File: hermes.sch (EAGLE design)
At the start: 36 parts

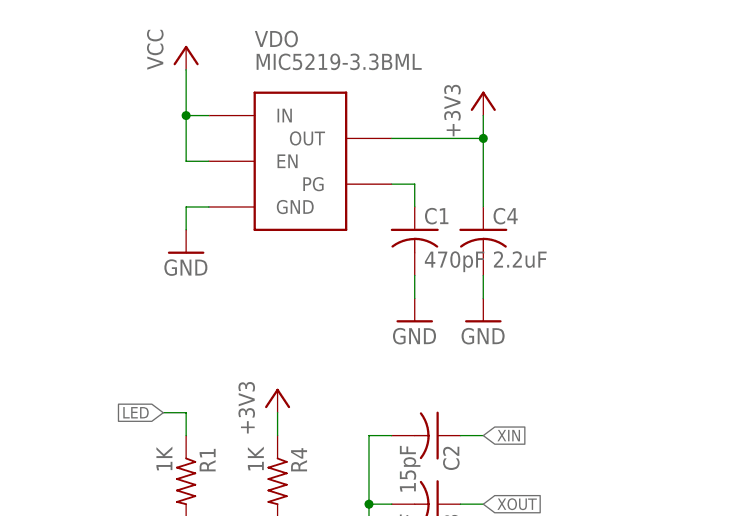
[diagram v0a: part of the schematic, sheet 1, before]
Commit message: Alternative version with LDO TS9013
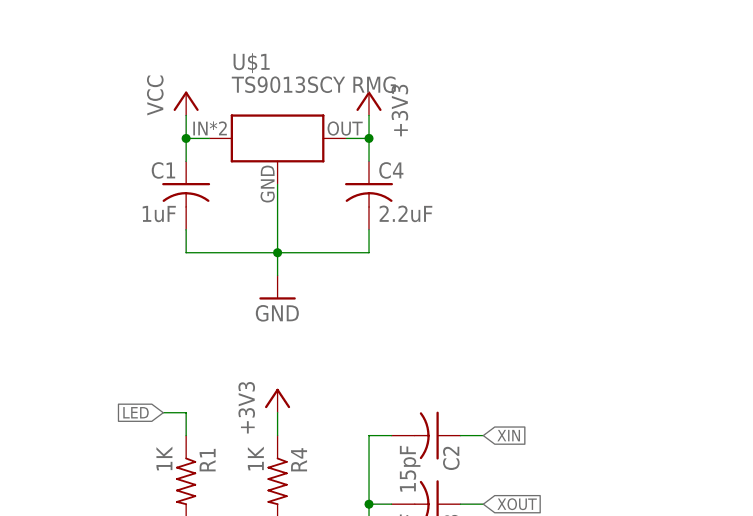
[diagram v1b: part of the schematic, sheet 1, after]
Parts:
- added U$1: TS9013SCY RMG, Hermes_lib:TS9013S
- C1: value 470pF -> 1uF
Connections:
- removed net N$2: C1.1, VDOG$1.PG
- net +3V3: now also U$1.P$2; no longer VDOG$1.OUT
- net GND: now also U$1.P$3; no longer VDOG$1.GND
- net VCC: now also C1.1, U$1.P$1; no longer VDOG$1.EN, VDOG$1.IN
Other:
- moved on the sheet: C1, C4
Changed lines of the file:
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@@
 <part name="P+1" library="supply1" library_urn="urn:adsk.eagle:library:371" deviceset="VCC" device=""/>
 <part name="GND8" library="supply1" library_urn="urn:adsk.eagle:library:371" deviceset="GND" device=""/>
-<part name="GND1" library="supply1" library_urn="urn:adsk.eagle:library:371" deviceset="GND" device=""/>
 <part name="+3V34" library="supply1" library_urn="urn:adsk.eagle:library:371" deviceset="+3V3" device=""/>
 <part name="LED1" library="eagle-ltspice" library_urn="urn:adsk.eagle:library:217" deviceset="LED_E" device="SML0603" package3d_urn="urn:adsk.eagle:package:13315/1"/>
@@
 <part name="FRAME2" library="frames" library_urn="urn:adsk.eagle:library:229" deviceset="A4L-LOC" device=""/>
 <part name="FRAME1" library="frames" library_urn="urn:adsk.eagle:library:229" deviceset="A4L-LOC" device=""/>
-<part name="C1" library="rcl" library_urn="urn:adsk.eagle:library:334" deviceset="C-US" device="C0201" package3d_urn="urn:adsk.eagle:package:23690/1" value="470pF"/>
-<part name="GND7" library="supply1" library_urn="urn:adsk.eagle:library:371" deviceset="GND" device=""/>
+<part name="C1" library="rcl" library_urn="urn:adsk.eagle:library:334" deviceset="C-US" device="C0201" package3d_urn="urn:adsk.eagle:package:23690/1" value="1uF"/>
 <part name="XTAL" library="Hermes_lib" deviceset="LFXTAL059596CUTT" device=""/>
 <part name="GND6" library="supply1" library_urn="urn:adsk.eagle:library:371" deviceset="GND" device=""/>
@@
 <part name="SLAVE" library="Hermes_lib" deviceset="PICO-BLADE8" device=""/>
 <part name="GND14" library="supply1" library_urn="urn:adsk.eagle:library:371" deviceset="GND" device=""/>
+<part name="U$1" library="Hermes_lib" deviceset="TS9013" device="S" value="TS9013SCY RMG "/>
 </parts>
 <sheets>
@@
 <instance part="C11" gate="G$1" x="172.72" y="139.7" rot="R90"/>
 <instance part="C9" gate="G$1" x="121.92" y="139.7" rot="R270"/>
-<instance part="VDO" gate="G$1" x="38.1" y="147.32"/>
-<instance part="C4" gate="G$1" x="58.42" y="139.7"/>
-<instance part="P+1" gate="VCC" x="25.4" y="160.02"/>
-<instance part="GND8" gate="1" x="58.42" y="129.54"/>
-<instance part="GND1" gate="1" x="25.4" y="137.16"/>
-<instance part="+3V34" gate="G$1" x="58.42" y="154.94"/>
+<instance part="C4" gate="G$1" x="45.72" y="144.78"/>
+<instance part="P+1" gate="VCC" x="25.4" y="154.94"/>
+<instance part="GND8" gate="1" x="35.56" y="132.08"/>
+<instance part="+3V34" gate="G$1" x="45.72" y="154.94" rot="MR0"/>
 <instance part="LED1" gate="G$1" x="25.4" y="101.6"/>
 <instance part="LED2" gate="G$1" x="35.56" y="101.6"/>
@@
 <instance part="R6" gate="G$1" x="48.26" y="68.58" rot="R90"/>
 <instance part="FRAME1" gate="G$1" x="0" y="0"/>
-<instance part="C1" gate="G$1" x="50.8" y="139.7"/>
-<instance part="GND7" gate="1" x="50.8" y="129.54"/>
+<instance part="C1" gate="G$1" x="25.4" y="144.78" rot="MR0"/>
 <instance part="XTAL" gate="G$1" x="53.34" y="97.79" rot="R180"/>
 <instance part="GND6" gate="1" x="45.72" y="91.44"/>
@@
 <instance part="GND14" gate="1" x="187.96" y="45.72"/>
 <instance part="VDO" gate="-DICE" x="185.42" y="66.04" rot="R180"/>
+<instance part="U$1" gate="G$1" x="35.56" y="149.86"/>
 </instances>
 <busses>
@@
 </segment>
 <segment>
-<pinref part="VDO" gate="G$1" pin="OUT"/>
 <pinref part="C4" gate="G$1" pin="1"/>
-<wire x1="48.26" y1="149.86" x2="58.42" y2="149.86" width="0.1524" layer="91"/>
-<wire x1="58.42" y1="149.86" x2="58.42" y2="142.24" width="0.1524" layer="91"/>
+<wire x1="45.72" y1="152.4" x2="45.72" y2="149.86" width="0.1524" layer="91"/>
 <pinref part="+3V34" gate="G$1" pin="+3V3"/>
-<wire x1="58.42" y1="152.4" x2="58.42" y2="149.86" width="0.1524" layer="91"/>
-<junction x="58.42" y="149.86"/>
+<pinref part="U$1" gate="G$1" pin="P$2"/>
+<wire x1="45.72" y1="149.86" x2="45.72" y2="147.32" width="0.1524" layer="91"/>
+<wire x1="43.18" y1="149.86" x2="45.72" y2="149.86" width="0.1524" layer="91"/>
+<junction x="45.72" y="149.86"/>
 </segment>
 <segment>
@@
 <pinref part="C4" gate="G$1" pin="2"/>
 <pinref part="GND8" gate="1" pin="GND"/>
-<wire x1="58.42" y1="134.62" x2="58.42" y2="132.08" width="0.1524" layer="91"/>
-</segment>
-<segment>
-<pinref part="GND1" gate="1" pin="GND"/>
-<pinref part="VDO" gate="G$1" pin="GND"/>
-<wire x1="25.4" y1="142.24" x2="25.4" y2="139.7" width="0.1524" layer="91"/>
-<wire x1="27.94" y1="142.24" x2="25.4" y2="142.24" width="0.1524" layer="91"/>
+<wire x1="45.72" y1="139.7" x2="45.72" y2="137.16" width="0.1524" layer="91"/>
+<wire x1="45.72" y1="137.16" x2="35.56" y2="137.16" width="0.1524" layer="91"/>
+<wire x1="35.56" y1="137.16" x2="35.56" y2="134.62" width="0.1524" layer="91"/>
+<pinref part="C1" gate="G$1" pin="2"/>
+<wire x1="25.4" y1="139.7" x2="25.4" y2="137.16" width="0.1524" layer="91"/>
+<wire x1="25.4" y1="137.16" x2="35.56" y2="137.16" width="0.1524" layer="91"/>
+<junction x="35.56" y="137.16"/>
+<pinref part="U$1" gate="G$1" pin="P$3"/>
+<wire x1="35.56" y1="144.78" x2="35.56" y2="137.16" width="0.1524" layer="91"/>
 </segment>
 <segment>
@@
 <wire x1="45.72" y1="106.68" x2="45.72" y2="109.22" width="0.1524" layer="91"/>
 <junction x="45.72" y="109.22"/>
-</segment>
-<segment>
-<pinref part="C1" gate="G$1" pin="2"/>
-<pinref part="GND7" gate="1" pin="GND"/>
-<wire x1="50.8" y1="134.62" x2="50.8" y2="132.08" width="0.1524" layer="91"/>
 </segment>
 <segment>
@@
 <segment>
 <pinref part="P+1" gate="VCC" pin="VCC"/>
-<pinref part="VDO" gate="G$1" pin="IN"/>
-<wire x1="27.94" y1="152.4" x2="25.4" y2="152.4" width="0.1524" layer="91"/>
-<wire x1="25.4" y1="152.4" x2="25.4" y2="157.48" width="0.1524" layer="91"/>
-<wire x1="25.4" y1="152.4" x2="25.4" y2="147.32" width="0.1524" layer="91"/>
-<wire x1="25.4" y1="147.32" x2="27.94" y2="147.32" width="0.1524" layer="91"/>
-<junction x="25.4" y="152.4"/>
-<pinref part="VDO" gate="G$1" pin="EN"/>
+<wire x1="25.4" y1="149.86" x2="25.4" y2="152.4" width="0.1524" layer="91"/>
+<pinref part="U$1" gate="G$1" pin="P$1"/>
+<wire x1="27.94" y1="149.86" x2="25.4" y2="149.86" width="0.1524" layer="91"/>
+<pinref part="C1" gate="G$1" pin="1"/>
+<wire x1="25.4" y1="147.32" x2="25.4" y2="149.86" width="0.1524" layer="91"/>
+<junction x="25.4" y="149.86"/>
 </segment>
 <segment>
@@
 </segment>
 </net>
-<net name="N$2" class="0">
-<segment>
-<pinref part="VDO" gate="G$1" pin="PG"/>
-<pinref part="C1" gate="G$1" pin="1"/>
-<wire x1="48.26" y1="144.78" x2="50.8" y2="144.78" width="0.1524" layer="91"/>
-<wire x1="50.8" y1="144.78" x2="50.8" y2="142.24" width="0.1524" layer="91"/>
-</segment>
-</net>

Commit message: Updated CAM and BOM according to new parts used
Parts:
- removed VDO: MIC5219-3.3BML, Hermes_lib:MIC5219-3.3BML
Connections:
- net GND: no longer VDO-DICE.P$1
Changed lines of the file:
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@@
 <part name="C11" library="rcl" library_urn="urn:adsk.eagle:library:334" deviceset="C-US" device="C0201" package3d_urn="urn:adsk.eagle:package:23690/1" value="1uF"/>
 <part name="C9" library="rcl" library_urn="urn:adsk.eagle:library:334" deviceset="C-US" device="C0201" package3d_urn="urn:adsk.eagle:package:23690/1" value="100nF"/>
-<part name="VDO" library="Hermes_lib" deviceset="MIC5219-" device="3.3BML"/>
 <part name="C4" library="rcl" library_urn="urn:adsk.eagle:library:334" deviceset="C-US" device="C0201" package3d_urn="urn:adsk.eagle:package:23690/1" value="2.2uF"/>
 <part name="P+1" library="supply1" library_urn="urn:adsk.eagle:library:371" deviceset="VCC" device=""/>
@@
 <instance part="SLAVE" gate="-DICE" x="185.42" y="50.8" rot="R180"/>
 <instance part="GND14" gate="1" x="187.96" y="45.72"/>
-<instance part="VDO" gate="-DICE" x="185.42" y="66.04" rot="R180"/>
 <instance part="U$1" gate="G$1" x="35.56" y="149.86"/>
 </instances>
@@
 <wire x1="185.42" y1="50.8" x2="187.96" y2="50.8" width="0.1524" layer="91"/>
 <junction x="187.96" y="50.8"/>
-<pinref part="VDO" gate="-DICE" pin="P$1"/>
-<wire x1="185.42" y1="66.04" x2="187.96" y2="66.04" width="0.1524" layer="91"/>
-<wire x1="187.96" y1="66.04" x2="187.96" y2="60.96" width="0.1524" layer="91"/>
-<junction x="187.96" y="60.96"/>
 </segment>
 </net>
